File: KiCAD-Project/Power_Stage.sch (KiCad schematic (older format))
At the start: 10 parts, among them Q501 IAUC120N06S5N017ATMA1, Q502 IAUC120N06S5N017ATMA1

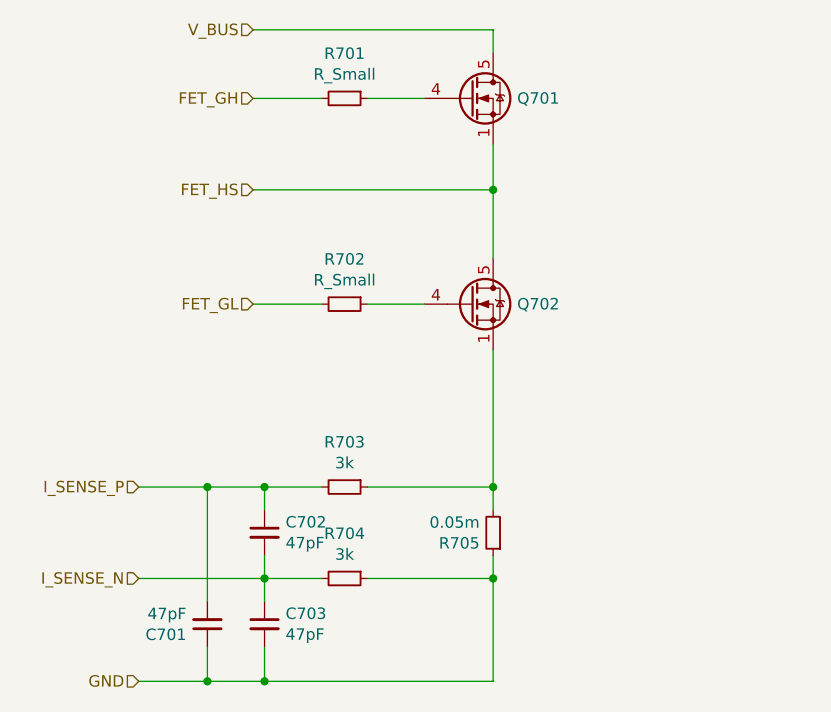
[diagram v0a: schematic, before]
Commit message: Schamtic package assigned
Package assigned, added two 100nF C's for temp sensors
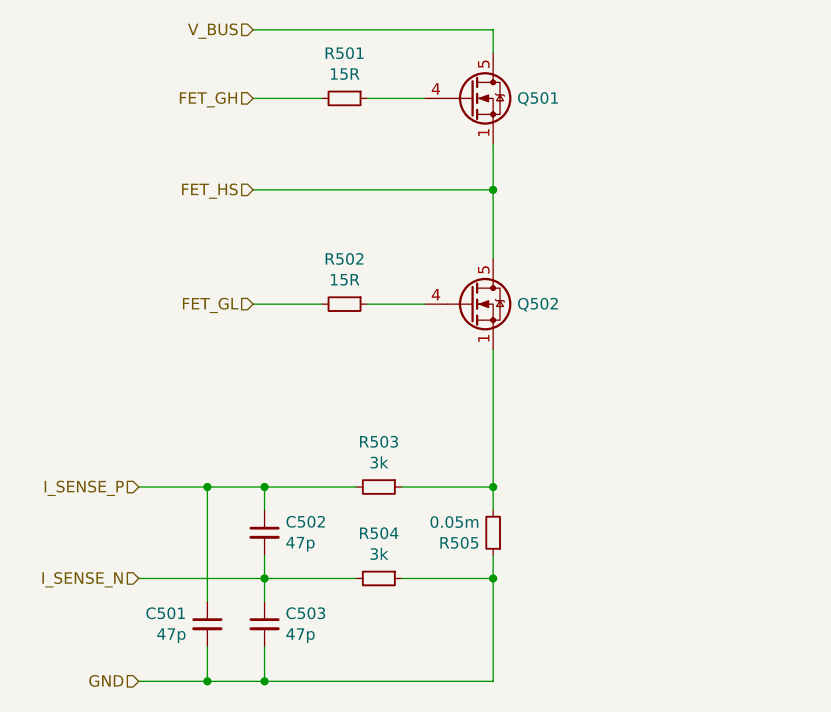
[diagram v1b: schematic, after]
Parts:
- C501, C502, C503: value 47pF -> 47p; footprint (none) -> Capacitor_SMD:C_0603_1608Metric
- R501, R502: value R_Small -> 15R; footprint (none) -> Resistor_SMD:R_0603_1608Metric
- R503, R504: footprint (none) -> Resistor_SMD:R_0603_1608Metric
- R505: footprint (none) -> Resistor_SMD:R_2010_5025Metric
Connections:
- net GND: now also C501.2; no longer C501.1
- net I_SENSE_P: now also C501.1; no longer C501.2
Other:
- moved on the sheet: R503, R504
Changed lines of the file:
@@
 AR Path="/60AFCC9B/617091B1/6168E3DC" Ref="Q601"  Part="1"
 AR Path="/60AFCC9B/6171E23C/6168E3DC" Ref="Q701"  Part="1"
-F 0 "Q701" H 5655 2300 50  0000 L CNN
+F 0 "Q501" H 5655 2300 50  0000 L CNN
 F 1 "IAUC120N06S5N017ATMA1" H 5655 2255 50  0001 L CNN
 F 2 "Package_TO_SOT_SMD:TDSON-8-1" H 5650 2225 50  0001 L CIN
@@
 L Device:R_Small R?
 U 1 1 6168E3F4
-P 4900 4400
+P 5050 4400
 AR Path="/6168E3F4" Ref="R?"  Part="1"
 AR Path="/60AFCC9B/6168E3F4" Ref="R?"  Part="1"
@@
 AR Path="/60AFCC9B/617091B1/6168E3F4" Ref="R604"  Part="1"
 AR Path="/60AFCC9B/6171E23C/6168E3F4" Ref="R704"  Part="1"
-F 0 "R704" V 4704 4400 50  0000 C CNN
-F 1 "3k" V 4795 4400 50  0000 C CNN
-F 2 "" H 4900 4400 50  0001 C CNN
-F 3 "~" H 4900 4400 50  0001 C CNN
-	1    4900 4400
+F 0 "R504" V 4854 4400 50  0000 C CNN
+F 1 "3k" V 4945 4400 50  0000 C CNN
+F 2 "Resistor_SMD:R_0603_1608Metric" H 5050 4400 50  0001 C CNN
+F 3 "~" H 5050 4400 50  0001 C CNN
+	1    5050 4400
 	0    1    1    0
 $EndComp
@@
 L Device:R_Small R?
 U 1 1 6168E3FA
-P 4900 4000
+P 5050 4000
 AR Path="/6168E3FA" Ref="R?"  Part="1"
 AR Path="/60AFCC9B/6168E3FA" Ref="R?"  Part="1"
@@
 AR Path="/60AFCC9B/617091B1/6168E3FA" Ref="R603"  Part="1"
 AR Path="/60AFCC9B/6171E23C/6168E3FA" Ref="R703"  Part="1"
-F 0 "R703" V 4704 4000 50  0000 C CNN
-F 1 "3k" V 4795 4000 50  0000 C CNN
-F 2 "" H 4900 4000 50  0001 C CNN
-F 3 "~" H 4900 4000 50  0001 C CNN
-	1    4900 4000
+F 0 "R503" V 4854 4000 50  0000 C CNN
+F 1 "3k" V 4945 4000 50  0000 C CNN
+F 2 "Resistor_SMD:R_0603_1608Metric" H 5050 4000 50  0001 C CNN
+F 3 "~" H 5050 4000 50  0001 C CNN
+	1    5050 4000
 	0    1    1    0
 $EndComp
@@
 AR Path="/60AFCC9B/617091B1/6168E40B" Ref="R605"  Part="1"
 AR Path="/60AFCC9B/6171E23C/6168E40B" Ref="R705"  Part="1"
-F 0 "R705" H 5609 4246 50  0000 L CNN
+F 0 "R505" H 5609 4246 50  0000 L CNN
 F 1 "0.05m" H 5609 4155 50  0000 L CNN
-F 2 "" H 5550 4200 50  0001 C CNN
+F 2 "Resistor_SMD:R_2010_5025Metric" H 5550 4200 50  0001 C CNN
 F 3 "~" H 5550 4200 50  0001 C CNN
 	1    5550 4200
@@
 AR Path="/60AFCC9B/617091B1/6168E411" Ref="C602"  Part="1"
 AR Path="/60AFCC9B/6171E23C/6168E411" Ref="C702"  Part="1"
-F 0 "C702" H 4642 4246 50  0000 L CNN
-F 1 "47pF" H 4642 4155 50  0000 L CNN
-F 2 "" H 4550 4200 50  0001 C CNN
+F 0 "C502" H 4642 4246 50  0000 L CNN
+F 1 "47p" H 4642 4155 50  0000 L CNN
+F 2 "Capacitor_SMD:C_0603_1608Metric" H 4550 4200 50  0001 C CNN
 F 3 "~" H 4550 4200 50  0001 C CNN
 	1    4550 4200
@@
 AR Path="/60AFCC9B/617091B1/6168E41D" Ref="C601"  Part="1"
 AR Path="/60AFCC9B/6171E23C/6168E41D" Ref="C701"  Part="1"
-F 0 "C701" H 4392 4646 50  0000 L CNN
-F 1 "47pF" H 4392 4555 50  0000 L CNN
-F 2 "" H 4300 4600 50  0001 C CNN
+F 0 "C501" H 4392 4646 50  0000 L CNN
+F 1 "47p" H 4392 4555 50  0000 L CNN
+F 2 "Capacitor_SMD:C_0603_1608Metric" H 4300 4600 50  0001 C CNN
 F 3 "~" H 4300 4600 50  0001 C CNN
 	1    4300 4600
-	-1   0    0    1
+	-1   0    0    -1
 $EndComp
 $Comp
@@
 AR Path="/60AFCC9B/617091B1/6168E423" Ref="C603"  Part="1"
 AR Path="/60AFCC9B/6171E23C/6168E423" Ref="C703"  Part="1"
-F 0 "C703" H 4642 4646 50  0000 L CNN
-F 1 "47pF" H 4642 4555 50  0000 L CNN
-F 2 "" H 4550 4600 50  0001 C CNN
+F 0 "C503" H 4642 4646 50  0000 L CNN
+F 1 "47p" H 4642 4555 50  0000 L CNN
+F 2 "Capacitor_SMD:C_0603_1608Metric" H 4550 4600 50  0001 C CNN
 F 3 "~" H 4550 4600 50  0001 C CNN
 	1    4550 4600
@@
 AR Path="/60AFCC9B/617091B1/6169E2C3" Ref="R601"  Part="1"
 AR Path="/60AFCC9B/6171E23C/6169E2C3" Ref="R701"  Part="1"
-F 0 "R701" V 4704 2300 50  0000 C CNN
-F 1 "R_Small" V 4795 2300 50  0000 C CNN
-F 2 "" H 4900 2300 50  0001 C CNN
+F 0 "R501" V 4704 2300 50  0000 C CNN
+F 1 "15R" V 4795 2300 50  0000 C CNN
+F 2 "Resistor_SMD:R_0603_1608Metric" H 4900 2300 50  0001 C CNN
 F 3 "~" H 4900 2300 50  0001 C CNN
 	1    4900 2300
@@
 AR Path="/60AFCC9B/617091B1/6168E405" Ref="Q602"  Part="1"
 AR Path="/60AFCC9B/6171E23C/6168E405" Ref="Q702"  Part="1"
-F 0 "Q702" H 5655 3200 50  0000 L CNN
+F 0 "Q502" H 5655 3200 50  0000 L CNN
 F 1 "IAUC120N06S5N017ATMA1" H 5655 3155 50  0001 L CNN
 F 2 "Package_TO_SOT_SMD:TDSON-8-1" H 5650 3125 50  0001 L CIN
@@
 	5550 3400 5550 4000
 Wire Wire Line
-	5000 4000 5550 4000
+	5150 4000 5550 4000
 Connection ~ 5550 4000
 Wire Wire Line
@@
 	5550 4300 5550 4400
 Wire Wire Line
-	5550 4400 5000 4400
+	5550 4400 5150 4400
 Wire Wire Line
 	5550 4400 5550 4850
@@
 	4550 4500 4550 4400
 Wire Wire Line
-	4550 4400 4800 4400
+	4550 4400 4950 4400
 Wire Wire Line
 	4550 4400 4550 4300
@@
 	4550 4100 4550 4000
 Wire Wire Line
-	4550 4000 4800 4000
+	4550 4000 4950 4000
 Wire Wire Line
 	4550 4000 4300 4000
@@
 AR Path="/60AFCC9B/617091B1/616C1AC5" Ref="R602"  Part="1"
 AR Path="/60AFCC9B/6171E23C/616C1AC5" Ref="R702"  Part="1"
-F 0 "R702" V 4704 3200 50  0000 C CNN
-F 1 "R_Small" V 4795 3200 50  0000 C CNN
-F 2 "" H 4900 3200 50  0001 C CNN
+F 0 "R502" V 4704 3200 50  0000 C CNN
+F 1 "15R" V 4795 3200 50  0000 C CNN
+F 2 "Resistor_SMD:R_0603_1608Metric" H 4900 3200 50  0001 C CNN
 F 3 "~" H 4900 3200 50  0001 C CNN
 	1    4900 3200

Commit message: pcb draft
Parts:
- added TP501: MotorConnector, MountingHole:MountingHole_4mm_Pad, symbol Connector:TestPoint
- R505: footprint Resistor_SMD:R_2010_5025Metric -> Resistor_SMD:R_2512_6332Metric
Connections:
- net FET_HS: now also TP501.1
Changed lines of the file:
@@
 $Descr A4 11693 8268
 encoding utf-8
-Sheet 5 7
+Sheet 6 7
 Title ""
 Date ""
@@
 AR Path="/60AFCC9B/617091B1/6168E3DC" Ref="Q601"  Part="1"
 AR Path="/60AFCC9B/6171E23C/6168E3DC" Ref="Q701"  Part="1"
-F 0 "Q501" H 5655 2300 50  0000 L CNN
+F 0 "Q601" H 5655 2300 50  0000 L CNN
 F 1 "IAUC120N06S5N017ATMA1" H 5655 2255 50  0001 L CNN
 F 2 "Package_TO_SOT_SMD:TDSON-8-1" H 5650 2225 50  0001 L CIN
@@
 AR Path="/60AFCC9B/617091B1/6168E3F4" Ref="R604"  Part="1"
 AR Path="/60AFCC9B/6171E23C/6168E3F4" Ref="R704"  Part="1"
-F 0 "R504" V 4854 4400 50  0000 C CNN
+F 0 "R604" V 4854 4400 50  0000 C CNN
 F 1 "3k" V 4945 4400 50  0000 C CNN
 F 2 "Resistor_SMD:R_0603_1608Metric" H 5050 4400 50  0001 C CNN
@@
 AR Path="/60AFCC9B/617091B1/6168E3FA" Ref="R603"  Part="1"
 AR Path="/60AFCC9B/6171E23C/6168E3FA" Ref="R703"  Part="1"
-F 0 "R503" V 4854 4000 50  0000 C CNN
+F 0 "R603" V 4854 4000 50  0000 C CNN
 F 1 "3k" V 4945 4000 50  0000 C CNN
 F 2 "Resistor_SMD:R_0603_1608Metric" H 5050 4000 50  0001 C CNN
@@
 AR Path="/60AFCC9B/617091B1/6168E40B" Ref="R605"  Part="1"
 AR Path="/60AFCC9B/6171E23C/6168E40B" Ref="R705"  Part="1"
-F 0 "R505" H 5609 4246 50  0000 L CNN
+F 0 "R605" H 5609 4246 50  0000 L CNN
 F 1 "0.05m" H 5609 4155 50  0000 L CNN
-F 2 "Resistor_SMD:R_2010_5025Metric" H 5550 4200 50  0001 C CNN
+F 2 "Resistor_SMD:R_2512_6332Metric" H 5550 4200 50  0001 C CNN
 F 3 "~" H 5550 4200 50  0001 C CNN
 	1    5550 4200
@@
 AR Path="/60AFCC9B/617091B1/6168E411" Ref="C602"  Part="1"
 AR Path="/60AFCC9B/6171E23C/6168E411" Ref="C702"  Part="1"
-F 0 "C502" H 4642 4246 50  0000 L CNN
+F 0 "C602" H 4642 4246 50  0000 L CNN
 F 1 "47p" H 4642 4155 50  0000 L CNN
 F 2 "Capacitor_SMD:C_0603_1608Metric" H 4550 4200 50  0001 C CNN
@@
 AR Path="/60AFCC9B/617091B1/6168E41D" Ref="C601"  Part="1"
 AR Path="/60AFCC9B/6171E23C/6168E41D" Ref="C701"  Part="1"
-F 0 "C501" H 4392 4646 50  0000 L CNN
+F 0 "C601" H 4392 4646 50  0000 L CNN
 F 1 "47p" H 4392 4555 50  0000 L CNN
 F 2 "Capacitor_SMD:C_0603_1608Metric" H 4300 4600 50  0001 C CNN
@@
 AR Path="/60AFCC9B/617091B1/6168E423" Ref="C603"  Part="1"
 AR Path="/60AFCC9B/6171E23C/6168E423" Ref="C703"  Part="1"
-F 0 "C503" H 4642 4646 50  0000 L CNN
+F 0 "C603" H 4642 4646 50  0000 L CNN
 F 1 "47p" H 4642 4555 50  0000 L CNN
 F 2 "Capacitor_SMD:C_0603_1608Metric" H 4550 4600 50  0001 C CNN
@@
 AR Path="/60AFCC9B/617091B1/6169E2C3" Ref="R601"  Part="1"
 AR Path="/60AFCC9B/6171E23C/6169E2C3" Ref="R701"  Part="1"
-F 0 "R501" V 4704 2300 50  0000 C CNN
+F 0 "R601" V 4704 2300 50  0000 C CNN
 F 1 "15R" V 4795 2300 50  0000 C CNN
 F 2 "Resistor_SMD:R_0603_1608Metric" H 4900 2300 50  0001 C CNN
@@
 AR Path="/60AFCC9B/617091B1/6168E405" Ref="Q602"  Part="1"
 AR Path="/60AFCC9B/6171E23C/6168E405" Ref="Q702"  Part="1"
-F 0 "Q502" H 5655 3200 50  0000 L CNN
+F 0 "Q602" H 5655 3200 50  0000 L CNN
 F 1 "IAUC120N06S5N017ATMA1" H 5655 3155 50  0001 L CNN
 F 2 "Package_TO_SOT_SMD:TDSON-8-1" H 5650 3125 50  0001 L CIN
@@
 AR Path="/60AFCC9B/617091B1/616C1AC5" Ref="R602"  Part="1"
 AR Path="/60AFCC9B/6171E23C/616C1AC5" Ref="R702"  Part="1"
-F 0 "R502" V 4704 3200 50  0000 C CNN
+F 0 "R602" V 4704 3200 50  0000 C CNN
 F 1 "15R" V 4795 3200 50  0000 C CNN
 F 2 "Resistor_SMD:R_0603_1608Metric" H 4900 3200 50  0001 C CNN
@@
 Wire Wire Line
 	5000 3200 5250 3200
+Wire Wire Line
+	5550 2700 6050 2700
+$Comp
+L Connector:TestPoint TP501
+U 1 1 60CA6E3A
+P 6050 2700
+AR Path="/60AFCC9B/61668C55/60CA6E3A" Ref="TP501"  Part="1"
+AR Path="/60AFCC9B/617091B1/60CA6E3A" Ref="TP601"  Part="1"
+AR Path="/60AFCC9B/6171E23C/60CA6E3A" Ref="TP701"  Part="1"
+F 0 "TP601" V 6004 2888 50  0000 L CNN
+F 1 "MotorConnector" V 6095 2888 50  0000 L CNN
+F 2 "MountingHole:MountingHole_4mm_Pad" H 6250 2700 50  0001 C CNN
+F 3 "~" H 6250 2700 50  0001 C CNN
+	1    6050 2700
+	0    1    1    0
+$EndComp
 $EndSCHEMATC
